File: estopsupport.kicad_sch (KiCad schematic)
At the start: 13 parts, among them J1 ESTOP1, J2 ESTOP2, J3 ${SIM.PARAMS}, J4 SYS_SIGSTOP, J5 5V_IN, J6 PWR, Q1 IRF540N, U1 PC817

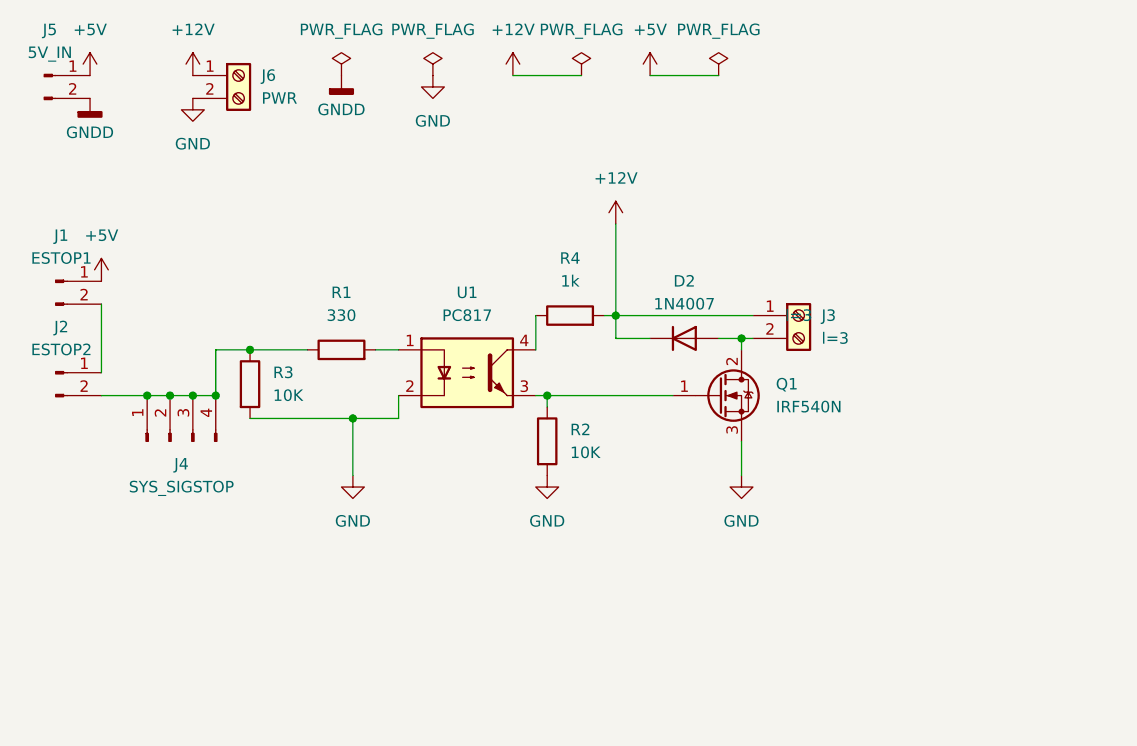
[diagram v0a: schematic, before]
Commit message: feat: add high side relay and suggestions from gemini
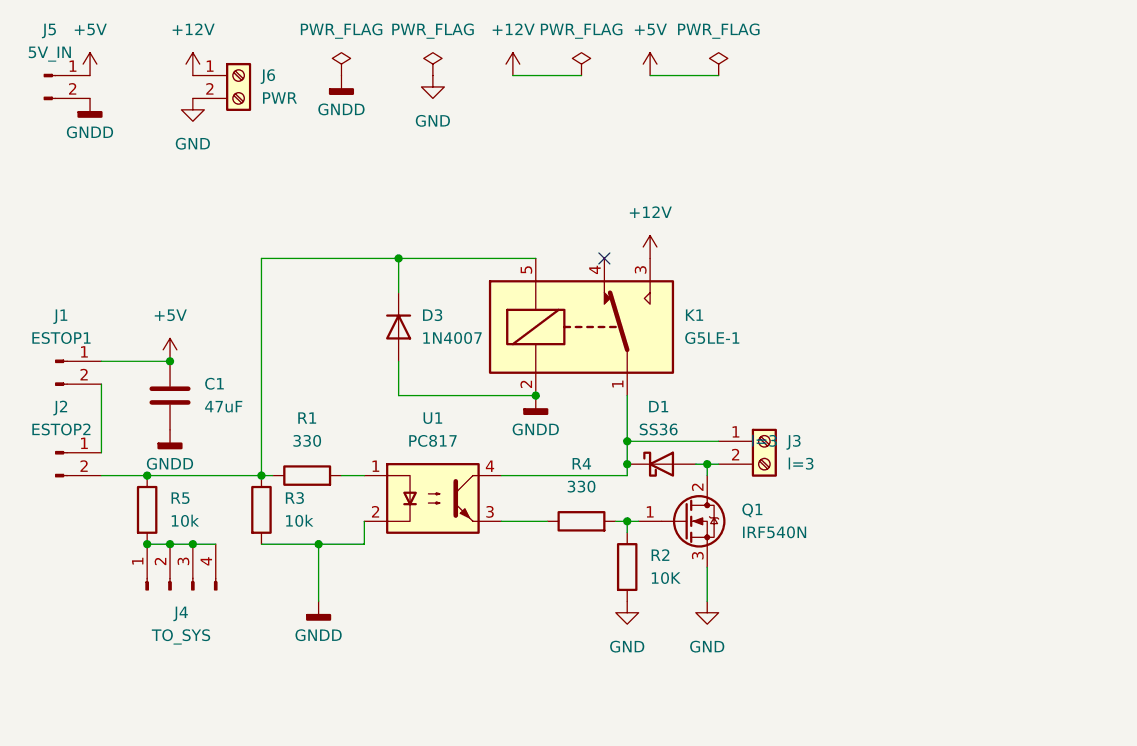
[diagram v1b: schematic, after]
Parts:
- removed D2: 1N4007, Diode_THT:D_DO-41_SOD81_P10.16mm_Horizontal, symbol Diode:1N4007
- added C1: 47uF, symbol Device:C
- added D1: SS36, Diode_SMD:D_SMA, symbol Diode:SS36
- added D3: 1N4007, Diode_THT:D_DO-41_SOD81_P10.16mm_Horizontal, symbol Diode:1N4007
- added K1: G5LE-1, Relay_THT:Relay_SPDT_Omron-G5LE-1, symbol Relay:G5LE-1
- added R5: 10k, symbol Device:R
- J4: value SYS_SIGSTOP -> TO_SYS
- R3: value 10K -> 10k
- R4: value 1k -> 330
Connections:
- net +12V: now also K1.3; no longer J3.1 (Pin_1), R4.2
- net +5V: now also C1.1
- net GND: no longer R3.2, U1.2
- net GNDD: now also R3.2, U1.2, C1.2, D3.2 (A), K1.2
- net at U1.4: now also J3.1 (Pin_1), D1.1 (K), K1.1; no longer R4.1
- net at J4.1 (Pin_1), J4.2 (Pin_2), J4.3 (Pin_3)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: now also R5.2; no longer J2.2 (Pin_2), R1.1, R3.1
- net at Q1.1 (G), R2.1: now also R4.2; no longer U1.3
- net at J3.2 (Pin_2), Q1.2 (D): now also D1.2 (A)
- new net: D3.1 (K), J2.2 (Pin_2), K1.5, R1.1, R3.1, R5.1
- new net: R4.1, U1.3
- no-connect marks 0 -> 1
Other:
- moved on the sheet: J1, J2, J3, J4, Q1, R1, R2, R3, U1

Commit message: feat: use a profet instead - simpler and more resistant to vibration. TBD: Connector footprint
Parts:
- removed C1: 47uF, symbol Device:C
- removed D3: 1N4007, Diode_THT:D_DO-41_SOD81_P10.16mm_Horizontal, symbol Diode:1N4007
- removed K1: G5LE-1, Relay_THT:Relay_SPDT_Omron-G5LE-1, symbol Relay:G5LE-1
- removed Q1: IRF540N, Package_TO_SOT_THT:TO-220-3_Vertical, symbol Transistor_FET:IRF540N
- added C1: 100u, Capacitor_SMD:CP_Elec_6.3x7.7, symbol Device:C_Polarized
- added C2: 100n, Capacitor_SMD:C_1206_3216Metric, symbol Device:C
- added D2: 1N4007, Diode_THT:D_DO-41_SOD81_P10.16mm_Horizontal, symbol Diode:1N4007
- added D3: LED, LED_THT:LED_D3.0mm, symbol Device:LED
- added J7: TAP_SENSE, Connector_PinHeader_2.54mm:PinHeader_1x04_P2.54mm_Vertical, symbol Connector:Conn_01x04_Pin
- added R6: 10k, Resistor_THT:R_Axial_DIN0207_L6.3mm_D2.5mm_P10.16mm_Horizontal, symbol Device:R
- added U2: BTS6163D, Package_TO_SOT_SMD:TO-252-4, symbol Power_Management:BTS6163D
- J1, J2, J5: footprint (none) -> Connector_PinHeader_2.54mm:PinHeader_1x02_P2.54mm_Horizontal
- J3: value ${SIM.PARAMS} -> CONTACTOR
- J4: value TO_SYS -> TAP_ESTOP; footprint (none) -> Connector_PinHeader_2.54mm:PinHeader_1x04_P2.54mm_Vertical
- R1, R3: footprint (none) -> Resistor_THT:R_Axial_DIN0207_L6.3mm_D2.5mm_P10.16mm_Horizontal
- R2: value 10K -> 6.2k; footprint (none) -> Resistor_THT:R_Axial_DIN0207_L6.3mm_D2.5mm_P10.16mm_Horizontal
- R4: value 330 -> 10k; footprint (none) -> Resistor_THT:R_Axial_DIN0207_L6.3mm_D2.5mm_P10.16mm_Horizontal
- R5: value 10k -> 3.3k; footprint (none) -> Resistor_THT:R_Axial_DIN0207_L6.3mm_D2.5mm_P10.16mm_Horizontal
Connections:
- net GNDD is gone; now on net GND: J5.2 (Pin_2), R3.2, U1.2
- net +12V: now also C1.1, C2.1, U2.3 (Vbb)
- net GND: now also D1.2 (A), J3.2 (Pin_2), R4.2, U1.3, C1.2, C2.2, R6.2; no longer R2.2
- net at D1.1 (K), J3.1 (Pin_1): now also U2.1 (OUT), U2.5 (OUT); no longer U1.4
- net at J2.2 (Pin_2), R1.1, R3.1: now also D2.2 (A); no longer R5.1
- net at R4.1: now also J7.1 (Pin_1), J7.2 (Pin_2), J7.3 (Pin_3), J7.4 (Pin_4), U2.4 (IS); no longer U1.3
- net at R2.1: now also D3.2 (A); no longer R4.2
- net at J4.1 (Pin_1), J4.2 (Pin_2), J4.3 (Pin_3)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: now also R6.1
- new net: R2.2, U2.2 (IN)
- new net: D3.1 (K), U1.4
- new net: D2.1 (K), R5.1
- no-connect marks 1 -> 0
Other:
- note added: "Note: Need adapter Output +12V Analog Current 0.33-7.5mA"
- note added: "To Kilovac"
- moved on the sheet: D1, J3, J4, R3, R5

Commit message: chore: finally settle on Phoenix Contact screw terminal
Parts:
- J3, J6: footprint (none) -> TerminalBlock_Phoenix:TerminalBlock_Phoenix_MKDS-1,5-2_1x02_P5.00mm_Horizontal
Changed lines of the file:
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@@
 			)
 		)
-		(property "Footprint" ""
+		(property "Footprint" "TerminalBlock_Phoenix:TerminalBlock_Phoenix_MKDS-1,5-2_1x02_P5.00mm_Horizontal"
 			(at 36.83 19.05 0)
 			(hide yes)
@@
 			)
 		)
-		(property "Footprint" ""
+		(property "Footprint" "TerminalBlock_Phoenix:TerminalBlock_Phoenix_MKDS-1,5-2_1x02_P5.00mm_Horizontal"
 			(at 119.38 66.04 0)
 			(hide yes)

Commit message: refactor: don't rely on adapter board - just design for it to be manually serviced and checked via shunt resistor
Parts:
- removed J7: TAP_SENSE, Connector_PinHeader_2.54mm:PinHeader_1x04_P2.54mm_Vertical, symbol Connector:Conn_01x04_Pin
- added H1, H2, H3, H4: M3, MountingHole:MountingHole_3.2mm_M3, symbol Mechanical:MountingHole
- D2: footprint Diode_THT:D_DO-41_SOD81_P10.16mm_Horizontal -> Diode_SMD:D_SMA; symbol Diode:1N4007 -> Device:D
- J4: footprint Connector_PinHeader_2.54mm:PinHeader_1x04_P2.54mm_Vertical -> Connector_PinSocket_2.54mm:PinSocket_1x04_P2.54mm_Horizontal
- R1, R2, R3, R4, R5, R6: footprint Resistor_THT:R_Axial_DIN0207_L6.3mm_D2.5mm_P10.16mm_Horizontal -> Resistor_SMD:R_0603_1608Metric
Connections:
- net GND: no longer J5.2 (Pin_2), R3.2, R6.2, U1.2
- new net GNDD: J5.2 (Pin_2), R3.2, R6.2, U1.2
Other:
- note added: "Shunt for measuring fault Non-automated but simpler Nominal Isense is about 0.33 mA Fault Isense is >5 mA"
- note removed: "Note: Need adapter Output +12V Analog Current 0.33-7.5mA"
- company: (none) -> SUTD Organisation of Autonomous Robotics - UnderWater Unit
- title: (none) -> E-Stop Support Circuit
- moved on the sheet: R4

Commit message: refactor: use a tht resistor for the shunt - easier to probe and replace
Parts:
- R4: footprint Resistor_SMD:R_0603_1608Metric -> Resistor_THT:R_Axial_DIN0204_L3.6mm_D1.6mm_P7.62mm_Horizontal
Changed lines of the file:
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@@
 			)
 		)
-		(property "Footprint" "Resistor_SMD:R_0603_1608Metric"
+		(property "Footprint" "Resistor_THT:R_Axial_DIN0204_L3.6mm_D1.6mm_P7.62mm_Horizontal"
 			(at 80.772 73.66 90)
 			(hide yes)
